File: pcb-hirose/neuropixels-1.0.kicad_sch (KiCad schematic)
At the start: 15 parts, among them J2 FH23-45S-0.3SHW(05), U6 MAX40111ANT

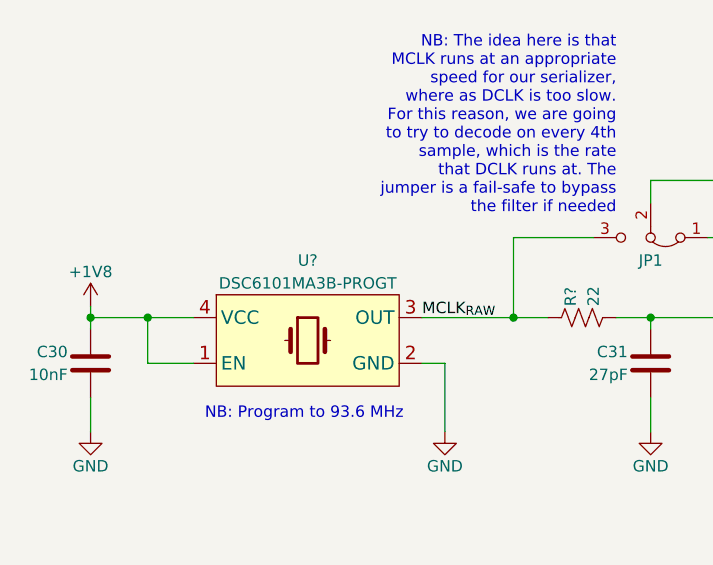
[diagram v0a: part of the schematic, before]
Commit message: Update oscillator part number to high-drive variant
- Orignal part number was too weak to reliably drive clock line on flex
  connector
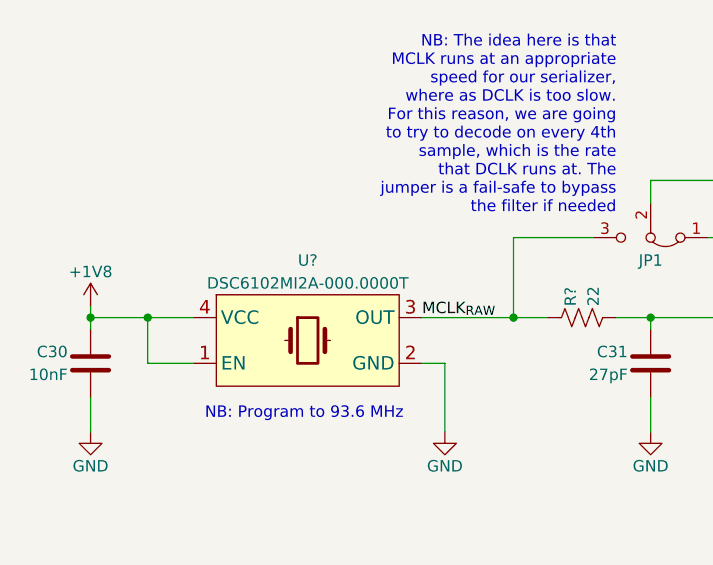
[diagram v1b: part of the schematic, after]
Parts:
- U?: value DSC6101MA3B-PROGT -> DSC6102MI2A-000.0000T
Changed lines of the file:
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@@
       (effects (font (size 1.27 1.27)))
     )
-    (property "Value" "DSC6101MA3B-PROGT" (at 77.47 127 0)
+    (property "Value" "DSC6102MI2A-000.0000T" (at 77.47 127 0)
       (effects (font (size 1.27 1.27)))
     )
